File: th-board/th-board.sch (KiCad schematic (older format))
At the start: 2 parts, among them U1 ESP-12F, U2 DHT11

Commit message: First version of pcb
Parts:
- added C1: C1uF, Capacitor_SMD:C_0805_2012Metric, symbol Device:C
- added C2: C10uF, Capacitor_SMD:C_0805_2012Metric, symbol Device:C
- added C3: C100uF, Capacitor_Tantalum_SMD:CP_EIA-6032-28_Kemet-C, symbol Device:CP
- added C4: C470pF, Capacitor_SMD:C_0805_2012Metric, symbol Device:C
- added D1: LED, symbol Device:LED
- added J1: Conn_01x02, Connector_PinHeader_2.54mm:PinHeader_1x02_P2.54mm_Vertical, symbol Connector_Generic:Conn_01x02
- added J2: Conn_01x04, Connector_PinHeader_2.54mm:PinHeader_1x04_P2.54mm_Vertical, symbol Connector_Generic:Conn_01x04
- added R1: R4K7, Resistor_SMD:R_0805_2012Metric, symbol Device:R
- added R10, R2, R7: R470, Resistor_SMD:R_0805_2012Metric, symbol Device:R
- added R3, R4, R5, R6, R8, R9: R12K, Resistor_SMD:R_0805_2012Metric, symbol Device:R
- added SW_Flash1, SW_User1, SW_User2: SW_Push, Button_Switch_SMD:SW_SPST_FSMSM, symbol Switch:SW_Push
- added U3: SPX3819M5-L, Package_TO_SOT_SMD:SOT-23-5, symbol Regulator_Linear:SPX3819M5-L
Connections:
- net DHT11_IO: now also R1.2
- net DHT11_VCC: now also R1.1
- net at U1.4 (GPIO16): now also R2.2; no longer U1.1 (~RST)
- net at U1.11 (GPIO9): now also R9.1, SW_User2.2
- net at U1.12 (GPIO10): now also R10.2
- net GND: now reaches U1.15 (GND), U2.4 (GND)
- net GND: now also C1.2, C2.2, C3.2, C4.2, D1.1 (K), J1.1 (Pin_1), J2.2 (Pin_2), R8.2, SW_Flash1.1, SW_User1.2, SW_User2.1, U3.2 (GND)
- net at U1.16 (GPIO15): now also R8.1
- net at U1.17 (GPIO2): now also R6.2
- net at U1.18 (GPIO0): now also R5.2, R7.1
- net RX: now reaches U1.21 (GPIO3/RXD)
- net RX: now also J2.3 (Pin_3)
- net TX: now reaches U1.22 (GPIO1/TXD)
- net TX: now also J2.4 (Pin_4)
- net at U1.3 (EN): now also R3.2
- net VCC: now reaches U1.8 (VCC)
- net VCC: now also C2.1, C3.1, R3.1, R4.1, R5.1, R6.1, R9.2, U3.5 (OUT)
- new net: R7.2, SW_Flash1.2
- new net: D1.2 (A), R10.1
- new net: C1.1, J1.2 (Pin_2), J2.1 (Pin_1), U3.1 (IN), U3.3 (EN)
- new net RST: C4.1, R2.1, R4.2, SW_User1.1, U1.1 (~RST)
- no-connect marks 1 -> 9
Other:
- moved on the sheet: U2

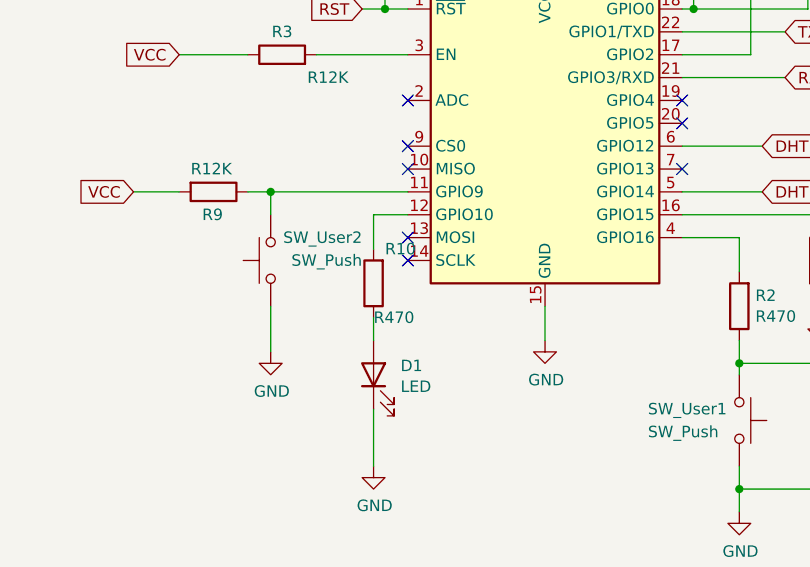
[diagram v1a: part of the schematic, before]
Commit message: Led added to pcb, v1.1
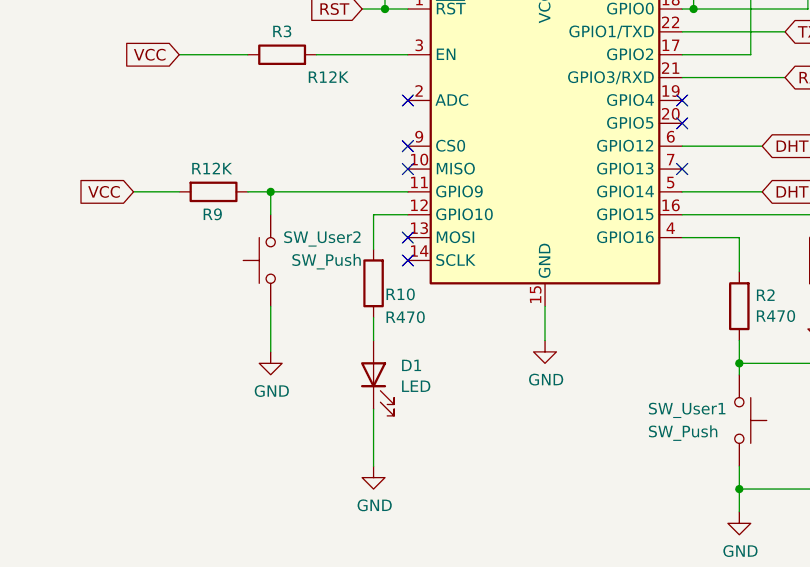
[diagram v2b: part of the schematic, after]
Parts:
- D1: footprint (none) -> LED_SMD:LED_0805_2012Metric
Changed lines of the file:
@@
 F 0 "D1" V 5589 4682 50  0000 R CNN
 F 1 "LED" V 5498 4682 50  0000 R CNN
-F 2 "" H 5550 4800 50  0001 C CNN
+F 2 "LED_SMD:LED_0805_2012Metric" H 5550 4800 50  0001 C CNN
 F 3 "~" H 5550 4800 50  0001 C CNN
 	1    5550 4800
@@
 U 1 1 61A7B13C
 P 5550 4400
-F 0 "R10" H 5500 4250 50  0000 R CNN
-F 1 "R470" H 5550 4550 50  0000 R CNN
+F 0 "R10" H 5500 4450 50  0000 R CNN
+F 1 "R470" H 5500 4550 50  0000 R CNN
 F 2 "Resistor_SMD:R_0805_2012Metric" V 5480 4400 50  0001 C CNN
 F 3 "~" H 5550 4400 50  0001 C CNN

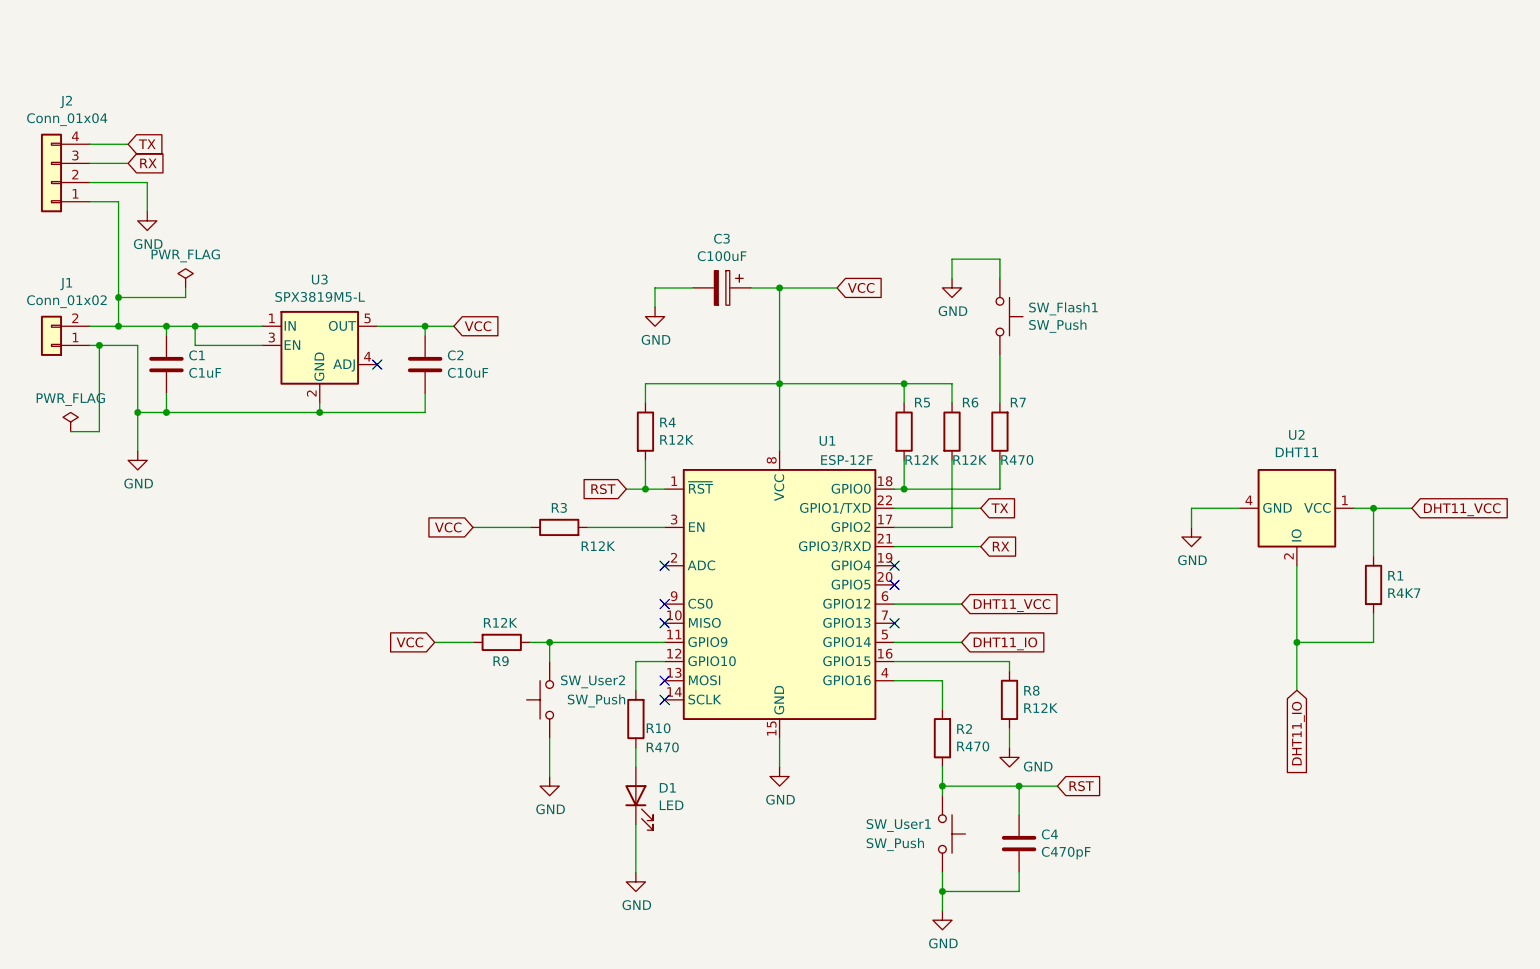
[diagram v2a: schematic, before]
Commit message: WEB: dashboards initial
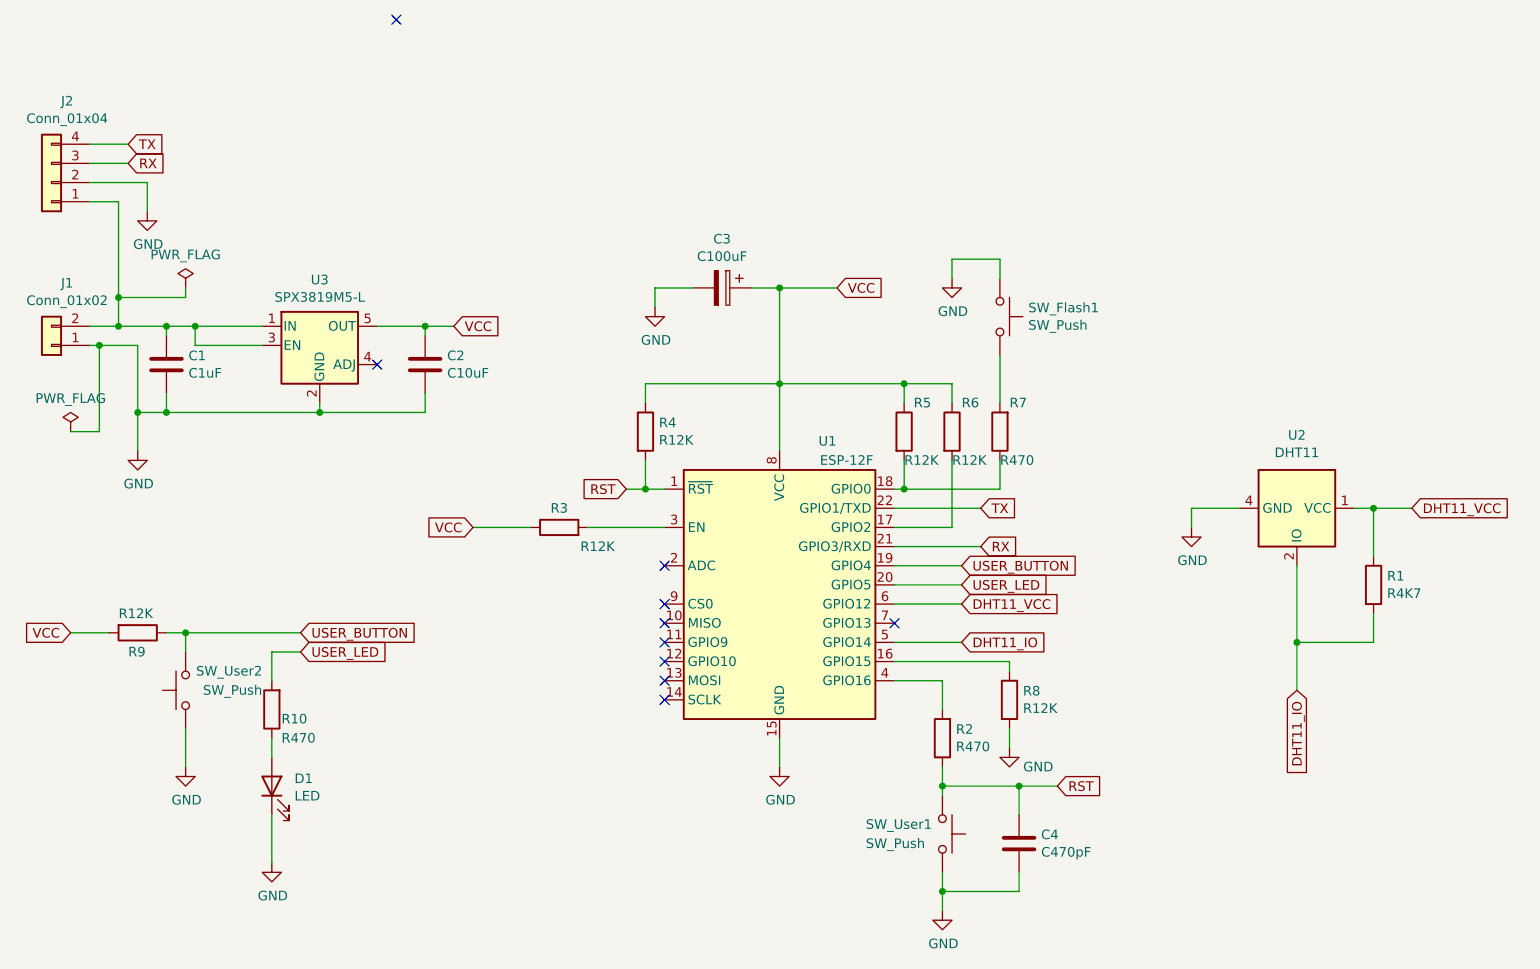
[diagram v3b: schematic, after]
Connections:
- net USER_BUTTON: now reaches R9.1, SW_User2.2
- net USER_BUTTON: now also U1.19 (GPIO4); no longer U1.11 (GPIO9)
- net at U1.12 (GPIO10): no longer R10.2
- net USER_LED: now reaches U1.20 (GPIO5)
- net USER_LED: now also R10.2
- no-connect marks 9 -> 10
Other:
- moved on the sheet: D1, R10, R9, SW_User2
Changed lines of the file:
@@
 NoConn ~ 5700 4200
 NoConn ~ 5700 4300
-NoConn ~ 6900 3700
-NoConn ~ 6900 3600
 $Comp
 L Switch:SW_Push SW_User2
 U 1 1 61A7DAE6
-P 5100 4300
-F 0 "SW_User2" V 5200 3900 50  0000 L CNN
-F 1 "SW_Push" V 5100 3900 50  0000 L CNN
-F 2 "Button_Switch_SMD:SW_SPST_FSMSM" H 5100 4500 50  0001 C CNN
-F 3 "~" H 5100 4500 50  0001 C CNN
-	1    5100 4300
+P 3200 4250
+F 0 "SW_User2" V 3300 3850 50  0000 L CNN
+F 1 "SW_Push" V 3200 3850 50  0000 L CNN
+F 2 "Button_Switch_SMD:SW_SPST_FSMSM" H 3200 4450 50  0001 C CNN
+F 3 "~" H 3200 4450 50  0001 C CNN
+	1    3200 4250
 	0    -1   -1   0
 $EndComp
 Wire Wire Line
-	5700 4000 5100 4000
+	3800 3950 3200 3950
 Wire Wire Line
-	5100 4000 5100 4100
+	3200 3950 3200 4050
 $Comp
 L Device:R R9
 U 1 1 61A823ED
-P 4850 4000
-F 0 "R9" V 4950 3950 50  0000 L CNN
-F 1 "R12K" V 4750 3900 50  0000 L CNN
-F 2 "Resistor_SMD:R_0805_2012Metric" V 4780 4000 50  0001 C CNN
-F 3 "~" H 4850 4000 50  0001 C CNN
-	1    4850 4000
+P 2950 3950
+F 0 "R9" V 3050 3900 50  0000 L CNN
+F 1 "R12K" V 2850 3850 50  0000 L CNN
+F 2 "Resistor_SMD:R_0805_2012Metric" V 2880 3950 50  0001 C CNN
+F 3 "~" H 2950 3950 50  0001 C CNN
+	1    2950 3950
 	0    1    1    0
 $EndComp
 Wire Wire Line
-	5000 4000 5100 4000
-Connection ~ 5100 4000
-Text GLabel 4500 4000 0    50   Input ~ 0
+	3100 3950 3200 3950
+Connection ~ 3200 3950
+Text GLabel 2600 3950 0    50   Input ~ 0
 VCC
 Wire Wire Line
-	4500 4000 4700 4000
+	2600 3950 2800 3950
 $Comp
 L power:GND #PWR02
 U 1 1 61A89564
-P 5100 4700
-F 0 "#PWR02" H 5100 4450 50  0001 C CNN
-F 1 "GND" H 5105 4527 50  0000 C CNN
-F 2 "" H 5100 4700 50  0001 C CNN
-F 3 "" H 5100 4700 50  0001 C CNN
-	1    5100 4700
+P 3200 4650
+F 0 "#PWR02" H 3200 4400 50  0001 C CNN
+F 1 "GND" H 3205 4477 50  0000 C CNN
+F 2 "" H 3200 4650 50  0001 C CNN
+F 3 "" H 3200 4650 50  0001 C CNN
+	1    3200 4650
 	1    0    0    -1
 $EndComp
 Wire Wire Line
-	5100 4700 5100 4500
+	3200 4650 3200 4450
 $Comp
 L Device:LED D1
 U 1 1 61A78EC7
-P 5550 4800
-F 0 "D1" V 5589 4682 50  0000 R CNN
-F 1 "LED" V 5498 4682 50  0000 R CNN
-F 2 "LED_SMD:LED_0805_2012Metric" H 5550 4800 50  0001 C CNN
-F 3 "~" H 5550 4800 50  0001 C CNN
-	1    5550 4800
+P 3650 4750
+F 0 "D1" V 3689 4632 50  0000 R CNN
+F 1 "LED" V 3598 4632 50  0000 R CNN
+F 2 "LED_SMD:LED_0805_2012Metric" H 3650 4750 50  0001 C CNN
+F 3 "~" H 3650 4750 50  0001 C CNN
+	1    3650 4750
 	0    -1   -1   0
 $EndComp
@@
 L Device:R R10
 U 1 1 61A7B13C
-P 5550 4400
-F 0 "R10" H 5500 4450 50  0000 R CNN
-F 1 "R470" H 5500 4550 50  0000 R CNN
-F 2 "Resistor_SMD:R_0805_2012Metric" V 5480 4400 50  0001 C CNN
-F 3 "~" H 5550 4400 50  0001 C CNN
-	1    5550 4400
+P 3650 4350
+F 0 "R10" H 3600 4400 50  0000 R CNN
+F 1 "R470" H 3600 4500 50  0000 R CNN
+F 2 "Resistor_SMD:R_0805_2012Metric" V 3580 4350 50  0001 C CNN
+F 3 "~" H 3650 4350 50  0001 C CNN
+	1    3650 4350
 	-1   0    0    1
 $EndComp
 Wire Wire Line
-	5550 4650 5550 4550
+	3650 4600 3650 4500
 Wire Wire Line
-	5550 4250 5550 4100
+	3650 4200 3650 4050
 Wire Wire Line
-	5550 4100 5700 4100
+	3650 4050 3800 4050
 $Comp
 L power:GND #PWR03
 U 1 1 61A81801
-P 5550 5200
-F 0 "#PWR03" H 5550 4950 50  0001 C CNN
-F 1 "GND" H 5555 5027 50  0000 C CNN
-F 2 "" H 5550 5200 50  0001 C CNN
-F 3 "" H 5550 5200 50  0001 C CNN
-	1    5550 5200
+P 3650 5150
+F 0 "#PWR03" H 3650 4900 50  0001 C CNN
+F 1 "GND" H 3655 4977 50  0000 C CNN
+F 2 "" H 3650 5150 50  0001 C CNN
+F 3 "" H 3650 5150 50  0001 C CNN
+	1    3650 5150
 	1    0    0    -1
 $EndComp
 Wire Wire Line
-	5550 4950 5550 5200
+	3650 4900 3650 5150
+Text GLabel 3800 3950 2    50   Input ~ 0
+USER_BUTTON
+Text GLabel 7250 3600 2    50   Input ~ 0
+USER_BUTTON
+Wire Wire Line
+	6900 3600 7250 3600
+Text GLabel 3800 4050 2    50   Input ~ 0
+USER_LED
+Text GLabel 7250 3700 2    50   Input ~ 0
+USER_LED
+Wire Wire Line
+	7250 3700 6900 3700
+NoConn ~ 5700 4000
+NoConn ~ 5700 4100
+NoConn ~ 4300 750
 $EndSCHEMATC

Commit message: PCB: very small pcb :)
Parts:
- removed SW_Flash1: SW_Push, Button_Switch_SMD:SW_SPST_FSMSM, symbol Switch:SW_Push
- added J3: Conn_01x02, Connector_PinHeader_2.54mm:PinHeader_1x02_P2.54mm_Vertical, symbol Connector_Generic:Conn_01x02
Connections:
- net GND: now also J3.1 (Pin_1)
- net at R7.2: now also J3.2 (Pin_2)
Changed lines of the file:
@@
 	7150 4750 7150 4800
-$Comp
-L Switch:SW_Push SW_Flash1
-U 1 1 61A5A31C
-P 7450 2300
-F 0 "SW_Flash1" V 7404 2448 50  0000 L CNN
-F 1 "SW_Push" V 7495 2448 50  0000 L CNN
-F 2 "Button_Switch_SMD:SW_SPST_FSMSM" H 7450 2500 50  0001 C CNN
-F 3 "~" H 7450 2500 50  0001 C CNN
-	1    7450 2300
-	0    1    1    0
-$EndComp
 $Comp
 L Device:R R7
@@
 Wire Wire Line
 	7200 2000 7450 2000
-Wire Wire Line
-	7450 2000 7450 2100
 Text GLabel 4700 3400 0    50   Input ~ 0
 VCC
@@
 	6950 3200 7450 3200
 Wire Wire Line
-	7450 2750 7450 2500
-Wire Wire Line
 	6300 2150 6600 2150
 Wire Wire Line
@@
 NoConn ~ 5700 4100
 NoConn ~ 4300 750
+$Comp
+L Connector_Generic:Conn_01x02 J3
+U 1 1 61C0EE98
+P 7650 2250
+F 0 "J3" H 7568 1925 50  0000 C CNN
+F 1 "Conn_01x02" H 7568 2016 50  0000 C CNN
+F 2 "Connector_PinHeader_2.54mm:PinHeader_1x02_P2.54mm_Vertical" H 7650 2250 50  0001 C CNN
+F 3 "~" H 7650 2250 50  0001 C CNN
+	1    7650 2250
+	1    0    0    -1
+$EndComp
+Wire Wire Line
+	7450 2350 7450 2750
+Wire Wire Line
+	7450 2000 7450 2250
 $EndSCHEMATC
